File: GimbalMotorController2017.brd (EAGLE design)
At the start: 90.5 x 80 mm, 125 parts, among them J1 SL03THROUGH_HOLE, J3 APP_2POS_CONFIG5V_HORIZ, Q7 MOSFET-PCHANNEL, Q8 MOSFET-PCHANNEL, Q9 MOSFET-NCHANNELAO3404A, U1 NUP4201MR6, U2 MAX3232D, U3 CSD18533Q5A, U4 CSD18533Q5A, U5 CSD18533Q5A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

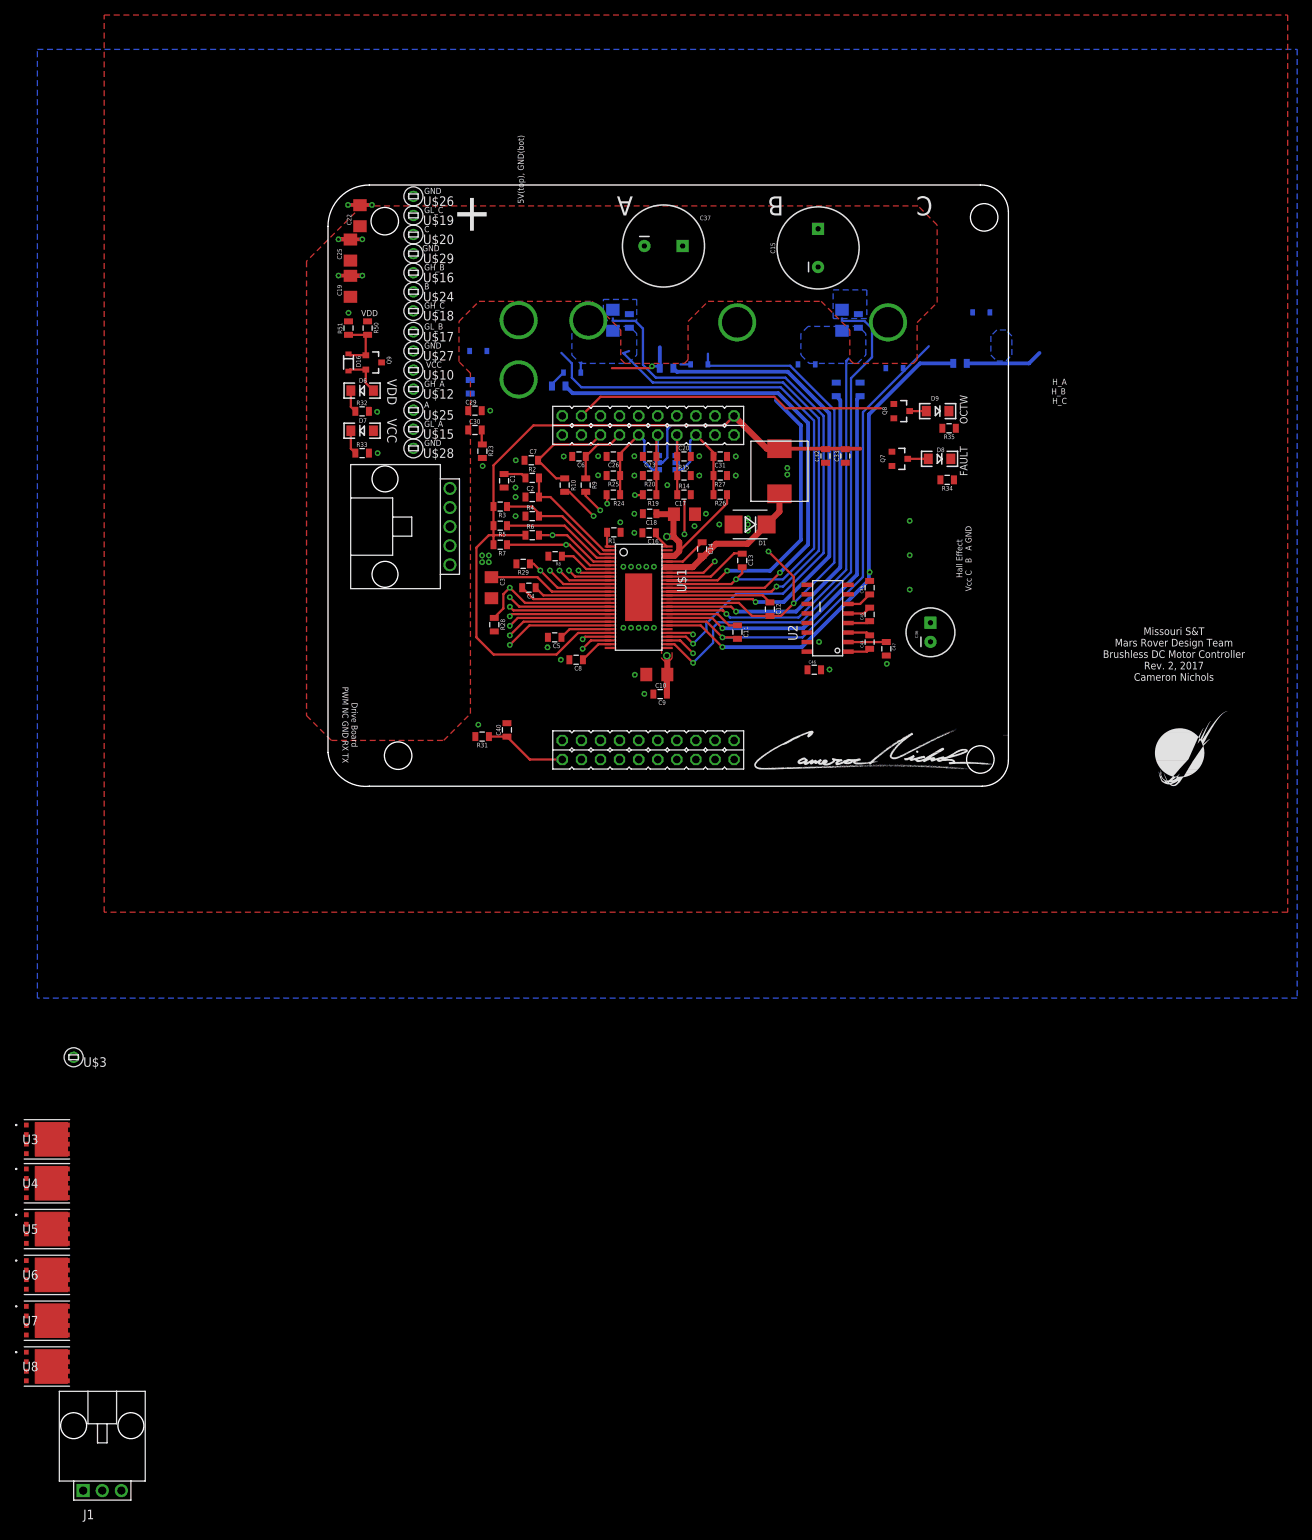
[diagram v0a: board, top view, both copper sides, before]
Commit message: Started routing traces on board
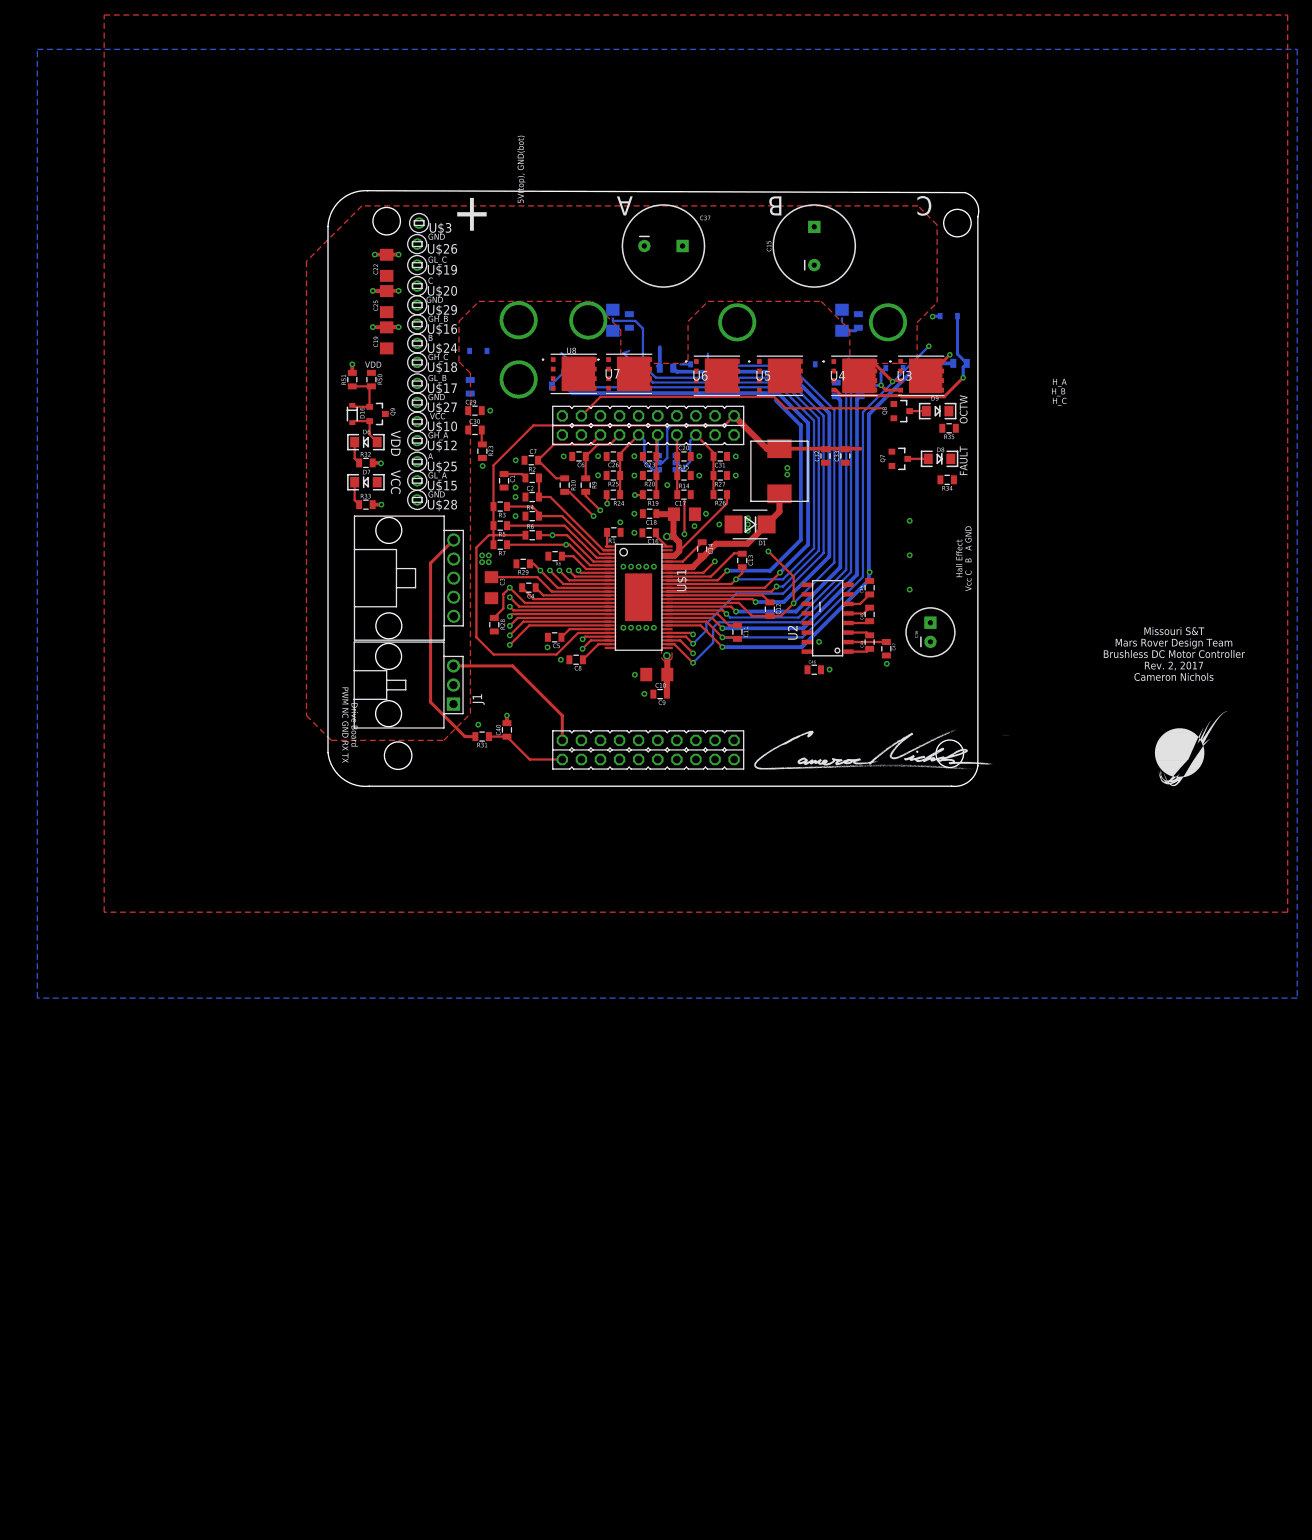
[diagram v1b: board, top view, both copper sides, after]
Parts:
- moved U3 154.5 mm to (88.4, 54.9)
- moved U4 151.9 mm to (79.5, 54.9)
- moved U5 149.7 mm to (69.6, 54.9)
- moved U8 149.5 mm to (42.2, 55.1)
- moved U6 149.2 mm to (61.2, 54.9)
- moved U7 147.9 mm to (49.5, 55.1)
- moved U$3 120.1 mm to (21.6, 75.2)
- moved J1 116.9 mm to (26.2, 13.7), turned to 90 degrees
- moved C19 8.39 mm to (17.3, 59.9)
- moved C25 8.39 mm to (17.3, 64.7)
- moved C22 7.50 mm to (17.3, 69.6)
- moved D16 6.88 mm to (12.7, 49.8)
- moved D7 6.88 mm to (14.5, 40.7)
- moved Q9 6.88 mm to (16.0, 49.8)
- moved U$15 6.88 mm to (21.3, 40.9)
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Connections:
- removed net N$37: U$3.P$1
- net PVDD: now also U$3.P$1
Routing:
- net N$34: track 0.00 -> 30.7 mm
- net PWM_IN_NO_FILTER: track 0.00 -> 20.5 mm
- net N$18: track 10.3 -> 27.5 mm, vias 0 -> 1
- net SP2: track 69.7 -> 57.5 mm
- net N$17: track 0.00 -> 8.35 mm, vias 0 -> 1
- net GND: track 12.9 -> 19.1 mm, vias 62 -> 64
- net N$14: track 10.7 -> 4.60 mm, vias 1 -> 0
- net SH_C: track 105.6 -> 110.4 mm, vias 2 -> 4
- net SL_B: track 66.8 -> 69.2 mm
- net PVDD: track 27.6 -> 29.1 mm, vias 2 -> 3
- removed copper zone on layer 16, net SL_A
- removed copper zone on layer 16, net SL_B
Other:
- board size 90.5 x 80 mm -> 86.6 x 79.3 mm

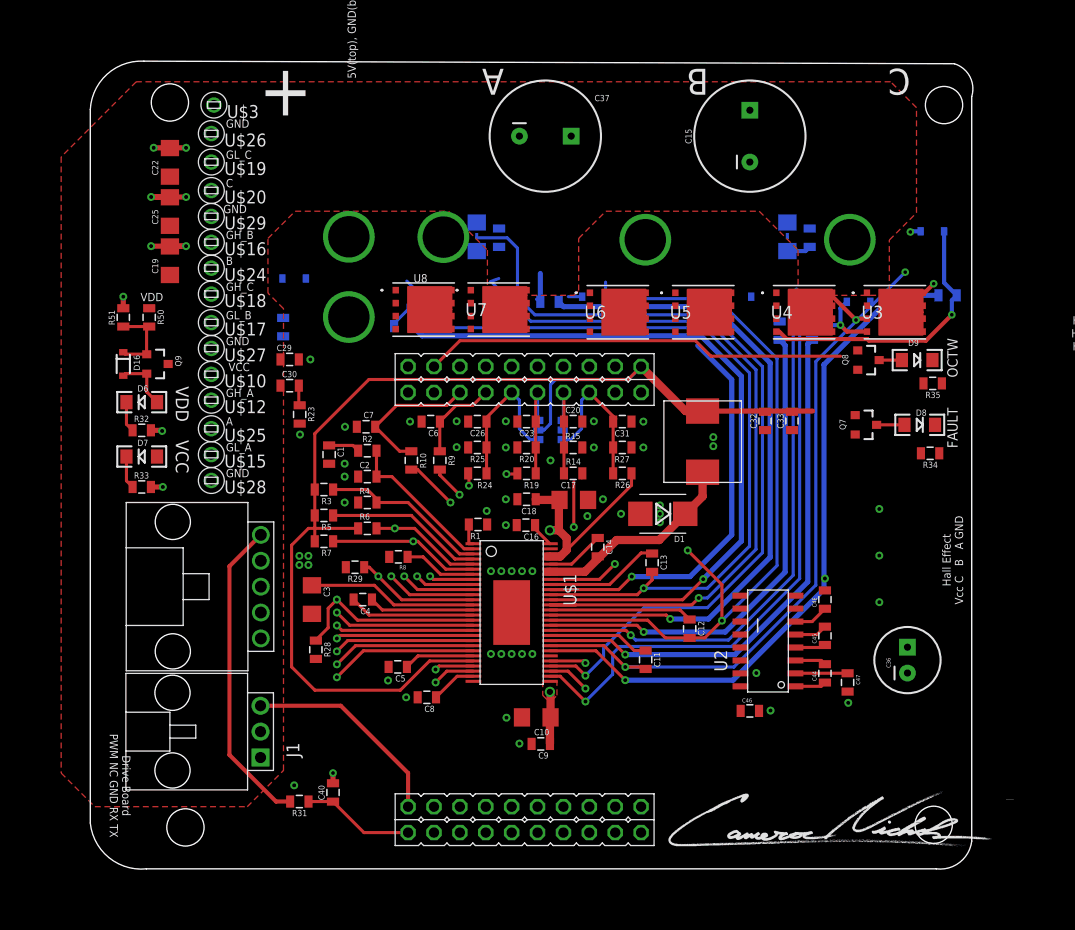
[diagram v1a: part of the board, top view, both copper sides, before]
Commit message: Updated silkscreen by removing hall effect sensor indicator and Cameron's signature, mounting holes were squared and board was straightened
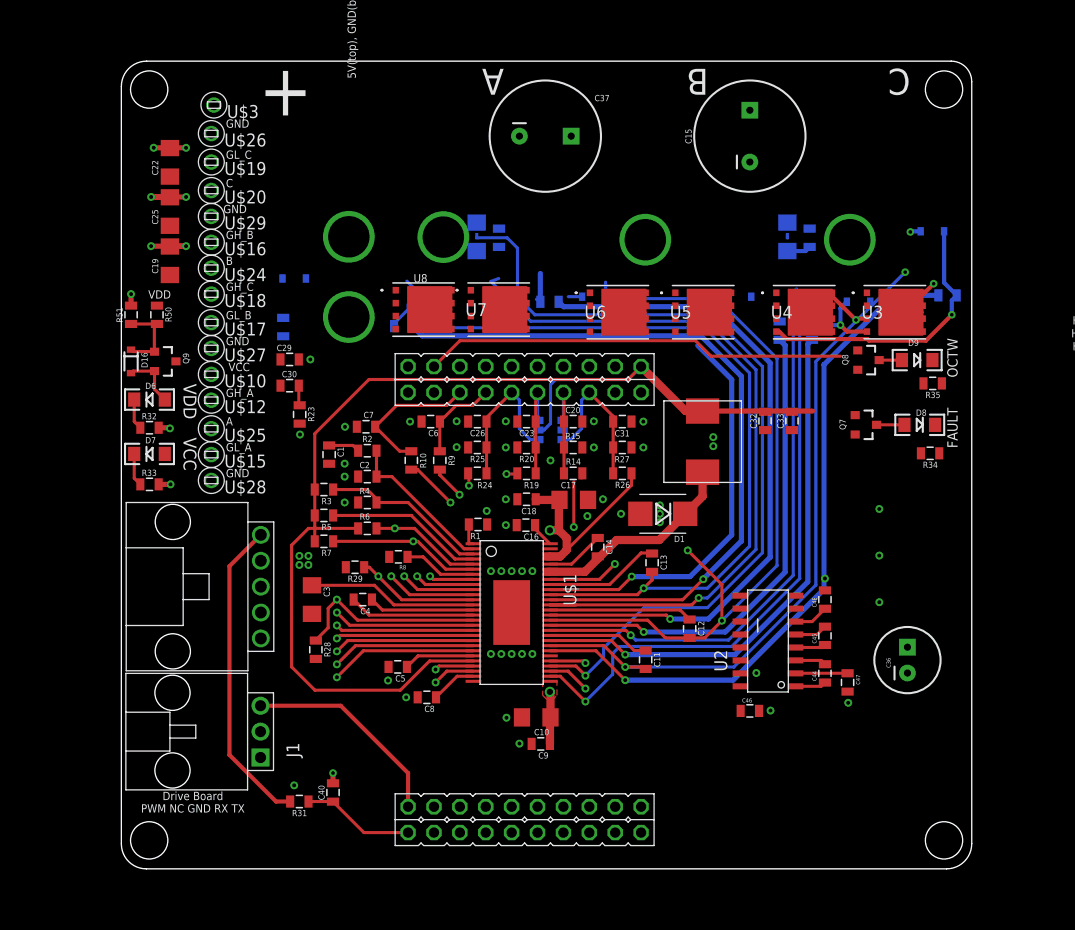
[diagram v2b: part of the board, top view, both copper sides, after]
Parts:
- moved D7 0.80 mm to (15.3, 41.0)
- moved D16 0.80 mm to (13.5, 50.0)
- moved D6 0.80 mm to (15.3, 46.3)
- moved Q9 0.80 mm to (16.8, 50.0)
- moved R32 0.80 mm to (15.3, 43.5)
- moved R33 0.80 mm to (15.3, 38.0)
- moved R51 0.80 mm to (13.5, 54.6)
- moved R50 0.80 mm to (16.0, 54.6)
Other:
- board size 86.6 x 79.3 mm -> 83.4 x 79.2 mm
- board text removed: "Hall Effect Vcc C B A GND"

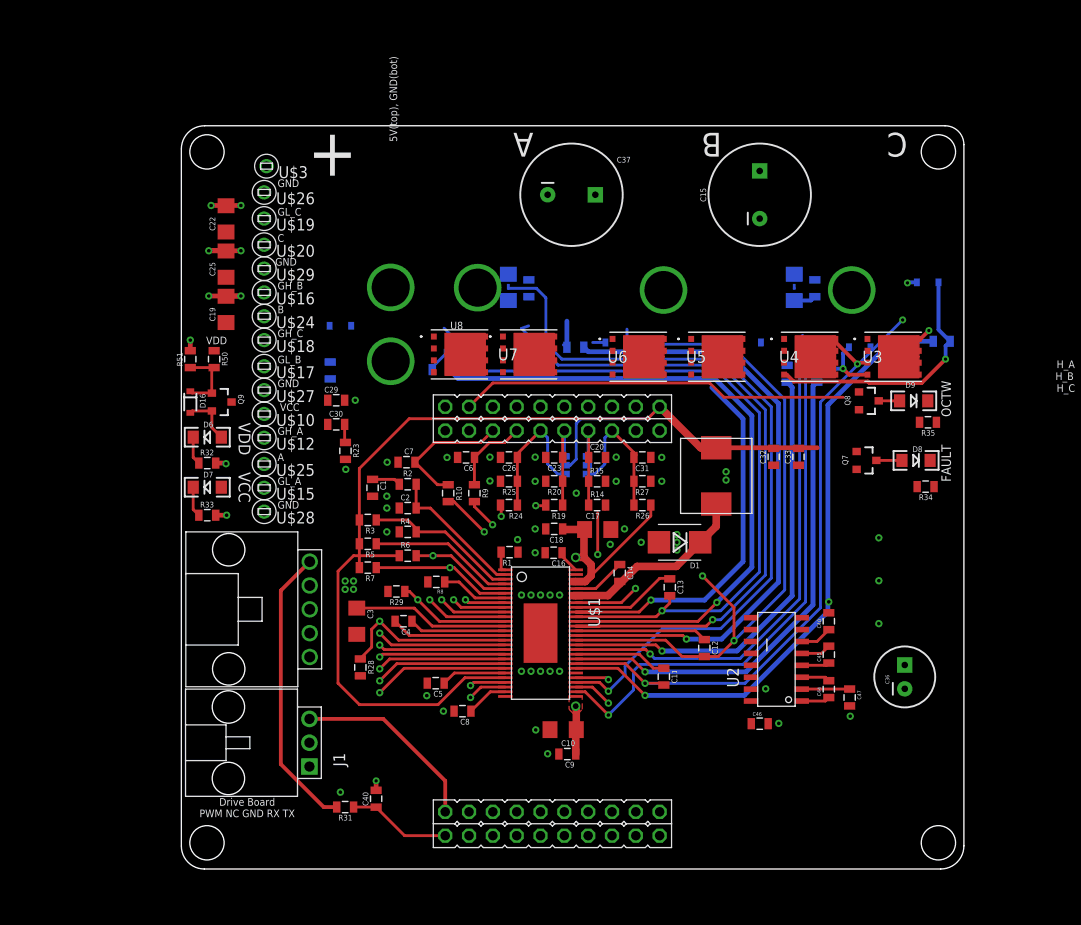
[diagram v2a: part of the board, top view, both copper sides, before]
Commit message: Testing a new board layout by moving the fets and andersons to the right of the board. MAX3232 has also been moved to the left closer to its connector
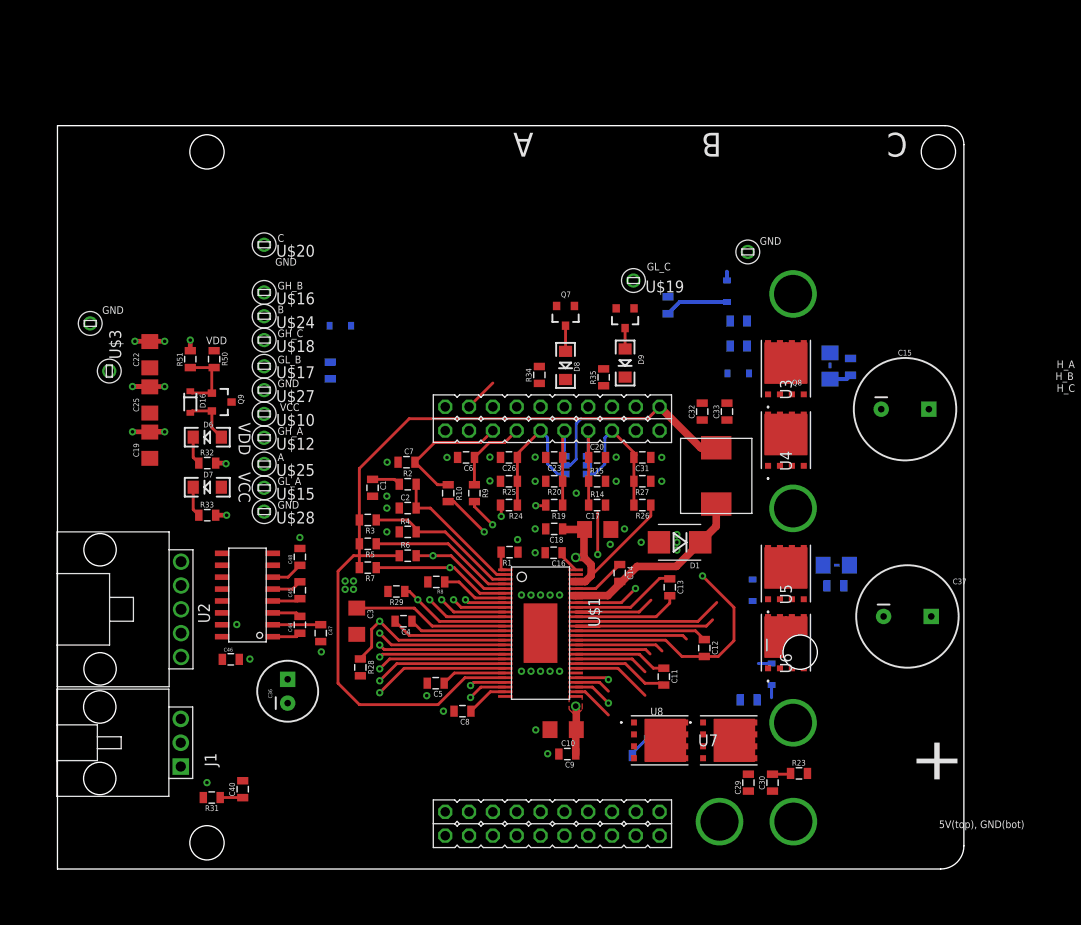
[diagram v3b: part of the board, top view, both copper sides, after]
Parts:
- moved J3 110.6 mm to (105.9, 9.24), turned to 180 degrees
- moved U$5 96.5 mm to (105.9, 19.8), turned to 180 degrees
- moved U$6 66.1 mm to (105.9, 42.7), turned to 180 degrees
- moved C36 65.8 mm to (23.8, 19.2)
- moved C30 60.2 mm to (75.5, 9.46), turned to 90 degrees
- moved C29 59.9 mm to (73.0, 9.46), turned to 90 degrees
- moved R23 59.3 mm to (78.4, 10.4), turned to 0 degrees
- moved C37 57.5 mm to (89.9, 27.2)
- moved C44 56.8 mm to (25.1, 26.3)
- moved C45 56.8 mm to (25.1, 30.0)
- moved C46 56.8 mm to (17.8, 22.6)
- moved C47 56.8 mm to (27.4, 25.4)
- moved C48 56.8 mm to (25.1, 33.5)
- moved U2 56.8 mm to (19.6, 29.5)
- moved U$29 51.6 mm to (72.9, 66.0)
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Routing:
- net SP1: track 81.1 -> 3.88 mm, vias 1 -> 0
- net SH_A: track 93.8 -> 26.3 mm, vias 2 -> 1
- net SH_C: track 110.4 -> 48.9 mm, vias 4 -> 1
- net GL_C: track 67.9 -> 8.59 mm, vias 1 -> 0
- net GL_A: track 71.7 -> 15.9 mm, vias 1 -> 0
- net SL_A: track 91.8 -> 36.2 mm, vias 2 -> 1
- net GH_B: track 66.6 -> 12.0 mm, vias 1 -> 0
- net SP2: track 57.5 -> 4.53 mm, vias 1 -> 0
- net SH_B: track 97.4 -> 50.1 mm, vias 3 -> 2
- net SL_B: track 69.2 -> 22.2 mm, vias 2 -> 1
- net GH_C: track 52.7 -> 7.96 mm, vias 1 -> 0
- net GL_B: track 48.8 -> 9.48 mm, vias 1 -> 0
- net NFAULT: track 74.4 -> 36.5 mm
- net GH_A: track 42.4 -> 11.0 mm, vias 1 -> 0
- net N$34: track 30.7 -> 0.00 mm
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- removed copper zone on layer 2, net SH_A
- removed copper zone on layer 2, net SH_B
- removed copper zone on layer 2, net SH_C
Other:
- board size 83.4 x 79.2 mm -> 96.6 x 79.2 mm
- board text removed: "Drive Board PWM NC GND RX TX"
- board text removed: "FAULT"
- board text removed: "OCTW"

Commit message: Finished arranging test points, beginning traces
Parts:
- moved U$16 72.4 mm to (81.8, 21.8)
- moved U$27 60.2 mm to (64.5, 9.40)
- moved U$15 42.2 mm to (53.6, 13.7)
- moved U$12 39.3 mm to (41.9, 12.7)
- moved D13 32.5 mm to (54.6, 37.6)
- moved R11 30.0 mm to (52.5, 35.6)
- moved U$28 28.0 mm to (22.6, 10.4)
- moved U$17 22.8 mm to (42.9, 61.2)
- moved U$20 22.6 mm to (31.2, 46.5)
- moved U$18 21.8 mm to (43.2, 56.9)
- moved U$25 19.1 mm to (37.8, 53.1)
- moved U$24 16.2 mm to (34.5, 49.8)
- moved C10 4.44 mm to (48.9, 16.1)
- moved C9 4.44 mm to (49.3, 13.5)
- moved U$3 3.09 mm to (1.78, 53.8), turned to 0 degrees
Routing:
- net PVDD: track 27.6 -> 29.7 mm
